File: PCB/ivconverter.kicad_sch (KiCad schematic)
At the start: 9 parts, among them U3 OPA1612AxD

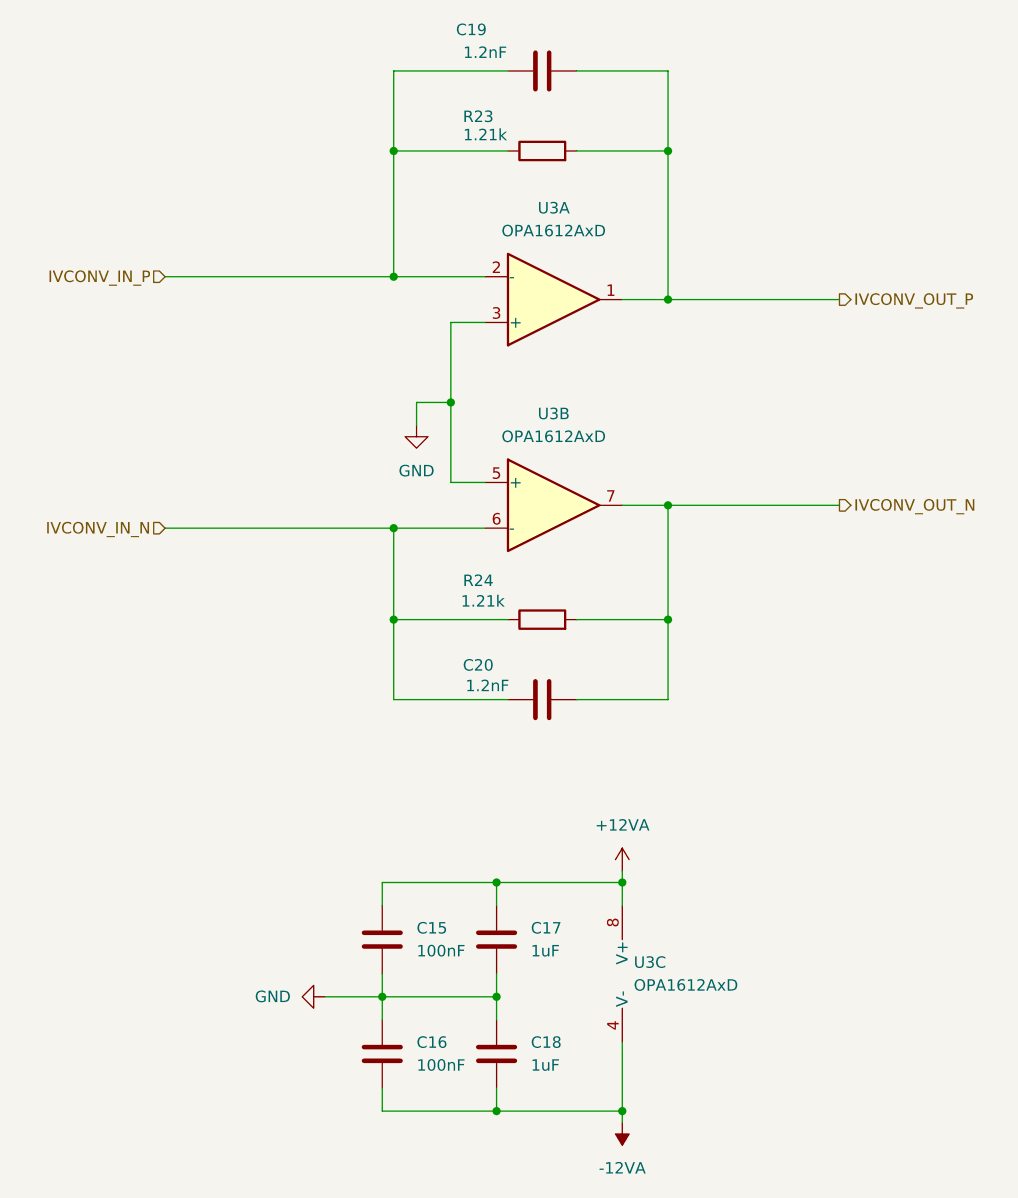
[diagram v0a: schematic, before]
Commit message: Added power supply and adjusted the AMP section to use only OPA1622 as output amp. In sync with Live 16
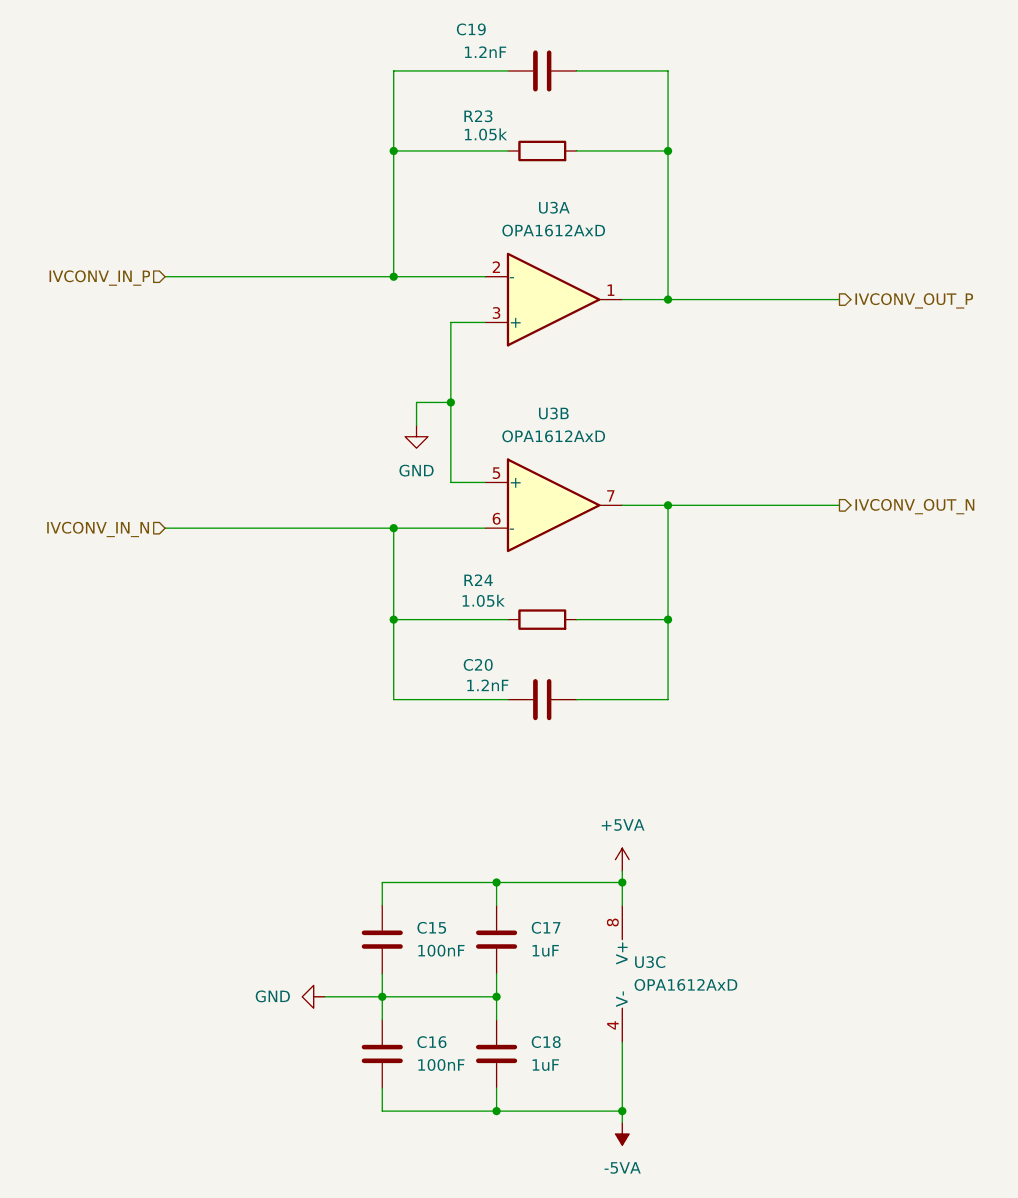
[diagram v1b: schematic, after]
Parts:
- C15, C16: Voltage 6.3V -> 25V
- C19, C20: Tolerance (none) -> 10%; Voltage (none) -> 25V
- R23, R24: value 1.21k -> 1.05k; Tolerance (none) -> 0.1%
- U3: footprint (none) -> Package_SO:SOIC-8_3.9x4.9mm_P1.27mm
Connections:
- net +12VA renamed +5VA
- net -12VA renamed -5VA
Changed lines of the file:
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@@
 			)
 		)
-		(property "Value" "1.21k"
+		(property "Value" "1.05k"
 			(at 143.256 105.918 90)
 			(effects
@@
 		)
 		(property "Description" "Resistor"
+			(at 149.86 107.95 0)
+			(effects
+				(font
+					(size 1.27 1.27)
+				)
+				(hide yes)
+			)
+		)
+		(property "Tolerance" "0.1%"
 			(at 149.86 107.95 0)
 			(effects
@@
 			)
 		)
-		(property "Voltage" "6.3V"
+		(property "Voltage" "25V"
 			(at 132.08 156.21 0)
 			(effects
@@
 			)
 		)
+		(property "Tolerance" "10%"
+			(at 149.86 116.84 0)
+			(effects
+				(font
+					(size 1.27 1.27)
+				)
+				(hide yes)
+			)
+		)
+		(property "Voltage" "25V"
+			(at 149.86 116.84 0)
+			(effects
+				(font
+					(size 1.27 1.27)
+				)
+				(hide yes)
+			)
+		)
 		(pin "2"
 		)
@@
 			)
 		)
+		(property "Tolerance" "10%"
+			(at 149.86 46.99 0)
+			(effects
+				(font
+					(size 1.27 1.27)
+				)
+				(hide yes)
+			)
+		)
+		(property "Voltage" "25V"
+			(at 149.86 46.99 0)
+			(effects
+				(font
+					(size 1.27 1.27)
+				)
+				(hide yes)
+			)
+		)
 		(pin "2"
 		)
@@
 			)
 		)
-		(property "Value" "1.21k"
+		(property "Value" "1.05k"
 			(at 143.51 54.102 90)
 			(effects
@@
 		)
 		(property "Description" "Resistor"
+			(at 149.86 55.88 0)
+			(effects
+				(font
+					(size 1.27 1.27)
+				)
+				(hide yes)
+			)
+		)
+		(property "Tolerance" "0.1%"
 			(at 149.86 55.88 0)
 			(effects
@@
 			)
 		)
-		(property "Value" "-12VA"
+		(property "Value" "-5VA"
 			(at 158.75 168.91 0)
 			(effects
@@
 			)
 		)
-		(property "Voltage" "6.3V"
+		(property "Voltage" "25V"
 			(at 132.08 143.51 0)
 			(effects
@@
 			)
 		)
-		(property "Footprint" ""
+		(property "Footprint" "Package_SO:SOIC-8_3.9x4.9mm_P1.27mm"
 			(at 151.13 95.25 0)
 			(effects
@@
 			)
 		)
-		(property "Footprint" ""
+		(property "Footprint" "Package_SO:SOIC-8_3.9x4.9mm_P1.27mm"
 			(at 161.29 147.32 0)
 			(effects
@@
 			)
 		)
-		(property "Footprint" ""
+		(property "Footprint" "Package_SO:SOIC-8_3.9x4.9mm_P1.27mm"
 			(at 151.13 72.39 0)
 			(effects
@@
 			)
 		)
-		(property "Value" "+12VA"
+		(property "Value" "+5VA"
 			(at 158.75 130.81 0)
 			(effects

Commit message: Added E2P and testpoints
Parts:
- C17, C18: footprint Capacitor_SMD:C_0402_1005Metric_Pad0.74x0.62mm_HandSolder -> Capacitor_SMD:C_0603_1608Metric_Pad1.08x0.95mm_HandSolder
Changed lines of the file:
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@@
 			)
 		)
-		(property "Footprint" "Capacitor_SMD:C_0402_1005Metric_Pad0.74x0.62mm_HandSolder"
+		(property "Footprint" "Capacitor_SMD:C_0603_1608Metric_Pad1.08x0.95mm_HandSolder"
 			(at 145.7452 147.32 0)
 			(effects
@@
 			)
 		)
-		(property "Footprint" "Capacitor_SMD:C_0402_1005Metric_Pad0.74x0.62mm_HandSolder"
+		(property "Footprint" "Capacitor_SMD:C_0603_1608Metric_Pad1.08x0.95mm_HandSolder"
 			(at 145.7452 160.02 0)
 			(effects

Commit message: Routing revised, added some missing parameters to components
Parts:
- C17, C18: Voltage 6.3V -> 16V
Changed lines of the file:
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@@
 			)
 		)
-		(property "Voltage" "6.3V"
+		(property "Voltage" "16V"
 			(at 144.78 143.51 0)
 			(effects
@@
 			)
 		)
-		(property "Voltage" "6.3V"
+		(property "Voltage" "16V"
 			(at 144.78 156.21 0)
 			(effects

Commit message: Updated PCB with digital traxce suggestions. Added JLCPCB Pns
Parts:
- C15, C16: JLCPCBPn (none) -> C1525; Voltage 25V -> 16V
- C17, C18: JLCPCBPn (none) -> C15849
- C19, C20: JLCPCBPn (none) -> C107021; Voltage 25V -> 50V
- U3: JLCPCBPn (none) -> C94590
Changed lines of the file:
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@@
 			)
 		)
-		(property "Voltage" "25V"
+		(property "Voltage" "16V"
+			(at 132.08 156.21 0)
+			(effects
+				(font
+					(size 1.27 1.27)
+				)
+				(hide yes)
+			)
+		)
+		(property "JLCPCBPn" "C1525"
 			(at 132.08 156.21 0)
 			(effects
@@
 			)
 		)
+		(property "JLCPCBPn" "C15849"
+			(at 144.78 143.51 0)
+			(effects
+				(font
+					(size 1.27 1.27)
+				)
+				(hide yes)
+			)
+		)
 		(pin "1"
 		)
@@
 			)
 		)
-		(property "Voltage" "25V"
+		(property "Voltage" "50V"
+			(at 149.86 116.84 0)
+			(effects
+				(font
+					(size 1.27 1.27)
+				)
+				(hide yes)
+			)
+		)
+		(property "JLCPCBPn" "C107021"
 			(at 149.86 116.84 0)
 			(effects
@@
 			)
 		)
-		(property "Voltage" "25V"
+		(property "Voltage" "50V"
+			(at 149.86 46.99 0)
+			(effects
+				(font
+					(size 1.27 1.27)
+				)
+				(hide yes)
+			)
+		)
+		(property "JLCPCBPn" "C107021"
 			(at 149.86 46.99 0)
 			(effects
@@
 			)
 		)
-		(property "Voltage" "25V"
+		(property "Voltage" "16V"
+			(at 132.08 143.51 0)
+			(effects
+				(font
+					(size 1.27 1.27)
+				)
+				(hide yes)
+			)
+		)
+		(property "JLCPCBPn" "C1525"
 			(at 132.08 143.51 0)
 			(effects
@@
 			)
 		)
+		(property "JLCPCBPn" "C15849"
+			(at 144.78 156.21 0)
+			(effects
+				(font
+					(size 1.27 1.27)
+				)
+				(hide yes)
+			)
+		)
 		(pin "1"
 		)
@@
 			)
 		)
+		(property "JLCPCBPn" "C94590"
+			(at 151.13 95.25 0)
+			(effects
+				(font
+					(size 1.27 1.27)
+				)
+				(hide yes)
+			)
+		)
 		(pin "3"
 		)
@@
 		)
 		(property "Description" "Dual SoundPlus High Performance, Bipolar-Input Audio Operational Amplifiers, SOIC-8"
+			(at 161.29 147.32 0)
+			(effects
+				(font
+					(size 1.27 1.27)
+				)
+				(hide yes)
+			)
+		)
+		(property "JLCPCBPn" "C94590"
 			(at 161.29 147.32 0)
 			(effects
@@
 			(at 151.13 72.39 0)
 			(effects
+				(font
+					(size 1.27 1.27)
+				)
+				(hide yes)
+			)
+		)
+		(property "JLCPCBPn" "C94590"
+			(at 151.13 72.39 0)
+			(effects

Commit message: Changed resistor values to match JLCPCB + general board revision
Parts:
- C19, C20: footprint Capacitor_SMD:C_0402_1005Metric_Pad0.74x0.62mm_HandSolder -> Capacitor_SMD:C_0603_1608Metric_Pad1.08x0.95mm_HandSolder; JLCPCBPn C107021 -> C576816
- R23, R24: JLCPCBPn (none) -> C2693047
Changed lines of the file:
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@@
+			)
+		)
+		(property "JLCPCBPn" "C2693047"
+			(at 149.86 107.95 0)
+			(effects
+				(font
+					(size 1.27 1.27)
+				)
+				(hide yes)
 			)
 		)
@@
 			)
 		)
-		(property "Footprint" "Capacitor_SMD:C_0402_1005Metric_Pad0.74x0.62mm_HandSolder"
+		(property "Footprint" "Capacitor_SMD:C_0603_1608Metric_Pad1.08x0.95mm_HandSolder"
 			(at 153.67 115.8748 0)
 			(effects
@@
 			)
 		)
-		(property "JLCPCBPn" "C107021"
+		(property "JLCPCBPn" "C576816"
 			(at 149.86 116.84 0)
 			(effects
@@
 			)
 		)
-		(property "Footprint" "Capacitor_SMD:C_0402_1005Metric_Pad0.74x0.62mm_HandSolder"
+		(property "Footprint" "Capacitor_SMD:C_0603_1608Metric_Pad1.08x0.95mm_HandSolder"
 			(at 153.67 46.0248 0)
 			(effects
@@
 			)
 		)
-		(property "JLCPCBPn" "C107021"
+		(property "JLCPCBPn" "C576816"
 			(at 149.86 46.99 0)
 			(effects
@@
 			(at 149.86 55.88 0)
 			(effects
+				(font
+					(size 1.27 1.27)
+				)
+				(hide yes)
+			)
+		)
+		(property "JLCPCBPn" "C2693047"
+			(at 149.86 55.88 0)
+			(effects

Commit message: Added filter capacitors to OPA1622 circuitry
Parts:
- C15, C16: JLCPCBPn C1525 -> (none); LCSC Part # (none) -> C1525
- C17, C18: JLCPCBPn C15849 -> (none); LCSC Part # (none) -> C15849
- C19, C20: JLCPCBPn C576816 -> (none); LCSC Part # (none) -> C576816
- R23, R24: JLCPCBPn C2693047 -> (none); LCSC Part # (none) -> C2693047
- U3: JLCPCBPn C94590 -> (none); LCSC Part # (none) -> C94590
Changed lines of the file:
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@@
 			)
 		)
-		(property "JLCPCBPn" "C2693047"
+		(property "LCSC Part #" "C2693047"
 			(at 149.86 107.95 0)
 			(effects
@@
 			)
 		)
-		(property "JLCPCBPn" "C1525"
+		(property "LCSC Part #" "C1525"
 			(at 132.08 156.21 0)
 			(effects
@@
 			)
 		)
-		(property "JLCPCBPn" "C15849"
+		(property "LCSC Part #" "C15849"
 			(at 144.78 143.51 0)
 			(effects
@@
 			)
 		)
-		(property "JLCPCBPn" "C576816"
+		(property "LCSC Part #" "C576816"
 			(at 149.86 116.84 0)
 			(effects
@@
 			)
 		)
-		(property "JLCPCBPn" "C576816"
+		(property "LCSC Part #" "C576816"
 			(at 149.86 46.99 0)
 			(effects
@@
 			)
 		)
-		(property "JLCPCBPn" "C2693047"
+		(property "LCSC Part #" "C2693047"
 			(at 149.86 55.88 0)
 			(effects
@@
 			)
 		)
-		(property "JLCPCBPn" "C1525"
+		(property "LCSC Part #" "C1525"
 			(at 132.08 143.51 0)
 			(effects
@@
 			)
 		)
-		(property "JLCPCBPn" "C15849"
+		(property "LCSC Part #" "C15849"
 			(at 144.78 156.21 0)
 			(effects
@@
 			)
 		)
-		(property "JLCPCBPn" "C94590"
+		(property "LCSC Part #" "C94590"
 			(at 151.13 95.25 0)
 			(effects
@@
 			)
 		)
-		(property "JLCPCBPn" "C94590"
+		(property "LCSC Part #" "C94590"
 			(at 161.29 147.32 0)
 			(effects
@@
 			)
 		)
-		(property "JLCPCBPn" "C94590"
+		(property "LCSC Part #" "C94590"
 			(at 151.13 72.39 0)
 			(effects

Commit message: Changed the BOM field for JLCPCB to the original name instead of LCSC
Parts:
- C15, C16: JLCPCB Part # (none) -> C1525; LCSC Part # C1525 -> (none)
- C17, C18: JLCPCB Part # (none) -> C15849; LCSC Part # C15849 -> (none)
- C19, C20: JLCPCB Part # (none) -> C576816; LCSC Part # C576816 -> (none)
- R23, R24: JLCPCB Part # (none) -> C2693047; LCSC Part # C2693047 -> (none)
- U3: JLCPCB Part # (none) -> C94590; LCSC Part # C94590 -> (none)
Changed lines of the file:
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@@
 			)
 		)
-		(property "LCSC Part #" "C2693047"
+		(property "JLCPCB Part #" "C2693047"
 			(at 149.86 107.95 0)
 			(effects
@@
 			)
 		)
-		(property "LCSC Part #" "C1525"
+		(property "JLCPCB Part #" "C1525"
 			(at 132.08 156.21 0)
 			(effects
@@
 			)
 		)
-		(property "LCSC Part #" "C15849"
+		(property "JLCPCB Part #" "C15849"
 			(at 144.78 143.51 0)
 			(effects
@@
 			)
 		)
-		(property "LCSC Part #" "C576816"
+		(property "JLCPCB Part #" "C576816"
 			(at 149.86 116.84 0)
 			(effects
@@
 			)
 		)
-		(property "LCSC Part #" "C576816"
+		(property "JLCPCB Part #" "C576816"
 			(at 149.86 46.99 0)
 			(effects
@@
 			)
 		)
-		(property "LCSC Part #" "C2693047"
+		(property "JLCPCB Part #" "C2693047"
 			(at 149.86 55.88 0)
 			(effects
@@
 			)
 		)
-		(property "LCSC Part #" "C1525"
+		(property "JLCPCB Part #" "C1525"
 			(at 132.08 143.51 0)
 			(effects
@@
 			)
 		)
-		(property "LCSC Part #" "C15849"
+		(property "JLCPCB Part #" "C15849"
 			(at 144.78 156.21 0)
 			(effects
@@
 			)
 		)
-		(property "LCSC Part #" "C94590"
+		(property "JLCPCB Part #" "C94590"
 			(at 151.13 95.25 0)
 			(effects
@@
 			)
 		)
-		(property "LCSC Part #" "C94590"
+		(property "JLCPCB Part #" "C94590"
 			(at 161.29 147.32 0)
 			(effects
@@
 			)
 		)
-		(property "LCSC Part #" "C94590"
+		(property "JLCPCB Part #" "C94590"
 			(at 151.13 72.39 0)
 			(effects
